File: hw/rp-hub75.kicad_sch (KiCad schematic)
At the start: 39 parts, among them J1 Display Connector, J2 USB_C_Receptacle_USB2.0_16P, J3 Screw_Terminal_01x02, J5 USB_A, J6 Conn_01x10, J7 Conn_01x05, J8 Conn_01x04, SW1 SW_Push, U1 AMS1117-3.3, U2 RP2350_60QFN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

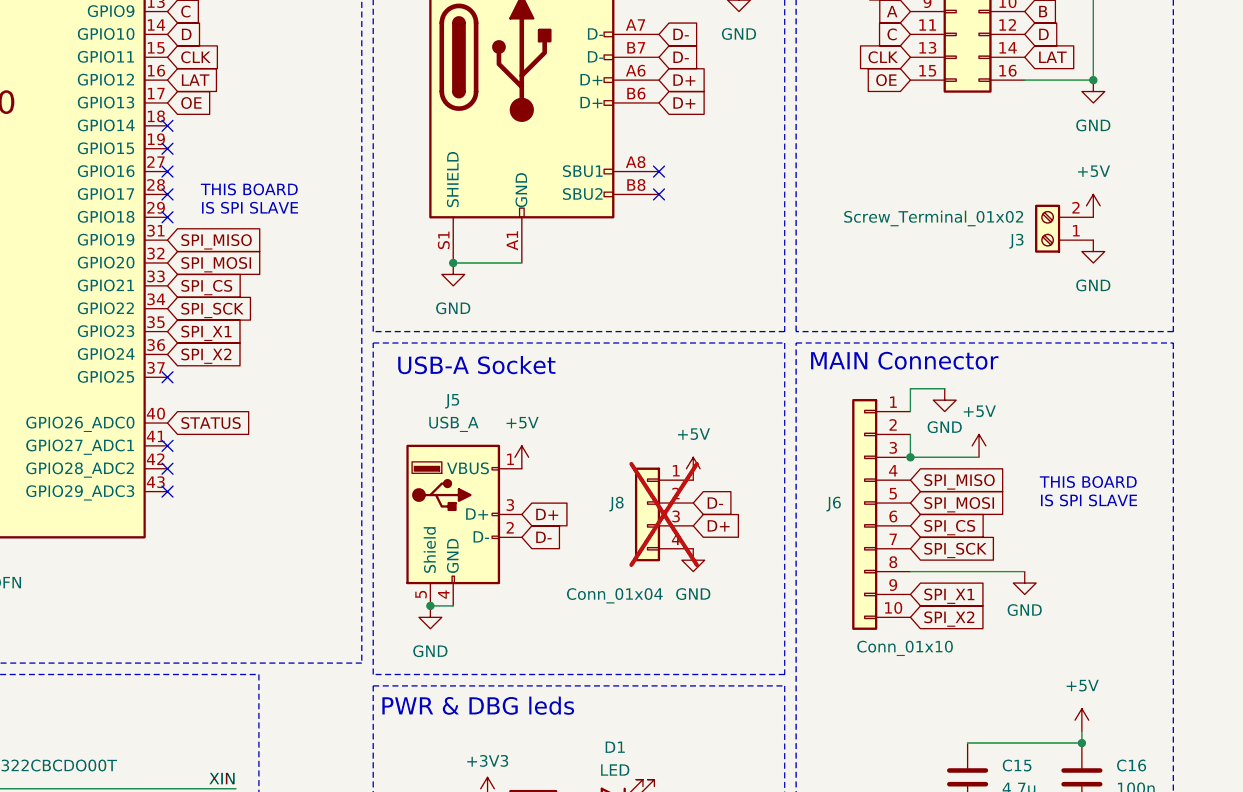
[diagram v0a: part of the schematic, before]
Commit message: v1.5 - use QSPI, better 1V1 line
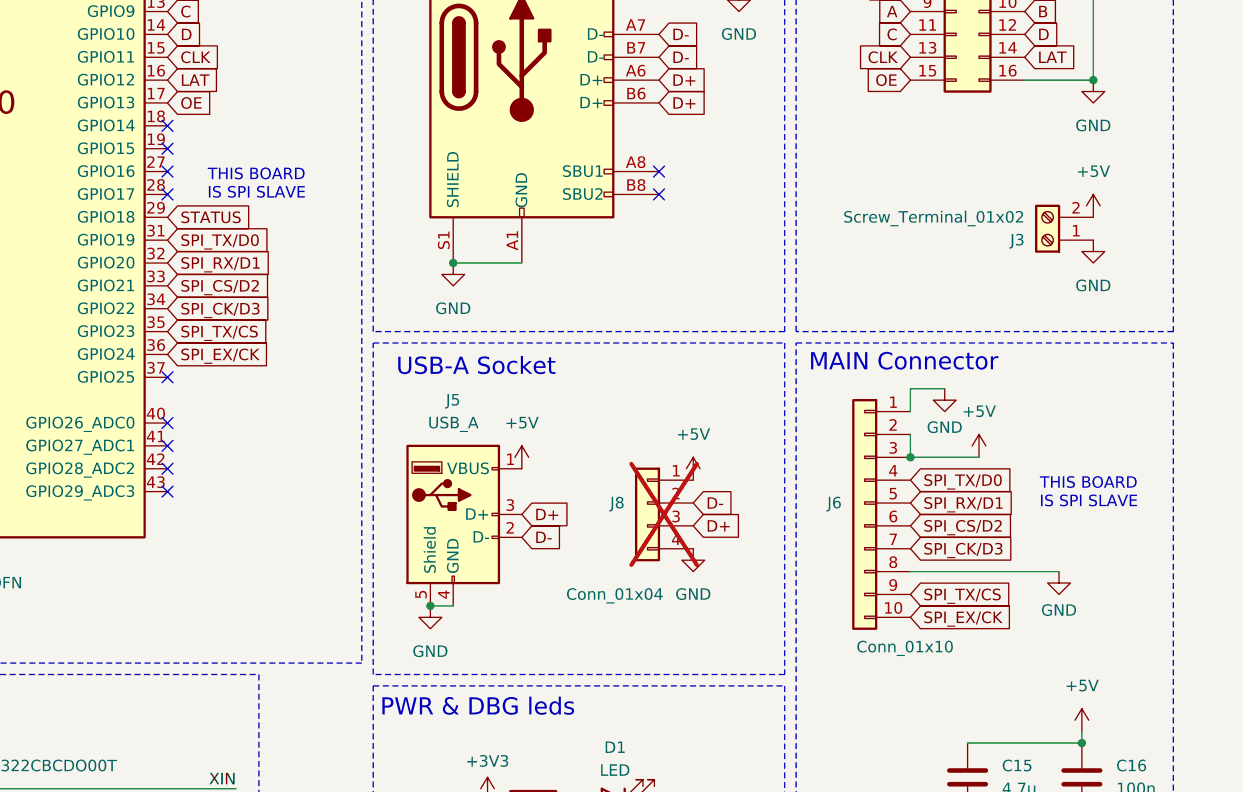
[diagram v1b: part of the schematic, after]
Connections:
- net STATUS: now also U2.29 (GPIO18); no longer U2.40 (GPIO26_ADC0)
- net SPI_CS renamed SPI_CS/D2
- net SPI_MISO renamed SPI_TX/D0
- net SPI_MOSI renamed SPI_RX/D1
- net SPI_SCK renamed SPI_CK/D3
- net SPI_X1 renamed SPI_TX/CS
- net SPI_X2 renamed SPI_EX/CK

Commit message: v1.6
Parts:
- removed J8: Conn_01x04, Connector_PinHeader_2.54mm:PinHeader_1x04_P2.54mm_Vertical, symbol Connector_Generic:Conn_01x04
- added J4: Conn_01x03, Connector_PinHeader_2.54mm:PinHeader_1x03_P2.54mm_Vertical, symbol Connector_Generic:Conn_01x03
- J3, J5: now not fitted
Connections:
- net GND: now also J4.1 (Pin_1)
- net SDA: now reaches U2.18 (GPIO14)
- net SDA: now also J4.3 (Pin_3)
- net SCL: now reaches U2.19 (GPIO15)
- net SCL: now also J4.2 (Pin_2)
- no-connect marks 11 -> 9

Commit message: v1.7
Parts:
- removed J6: Conn_01x10, Connector_JST:JST_XH_S10B-XH-A-1_1x10_P2.50mm_Horizontal, symbol Connector_Generic:Conn_01x10
- added J8: ZX-XH2.54-10PWT, Library:JST-XH-SMD-10Pin, symbol Connector_Generic_MountingPin:Conn_01x10_MountingPin
- J3: now fitted
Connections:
- net +5V: now also J8.2 (Pin_2), J8.3 (Pin_3)
- net GND: now also J8.1 (Pin_1), J8.8 (Pin_8), J8.MP (MountPin)
- net SPI_CK/D3: now also J8.7 (Pin_7)
- net SPI_CS/D2: now also J8.6 (Pin_6)
- net SPI_EX/CK: now also J8.10 (Pin_10)
- net SPI_RX/D1: now also J8.5 (Pin_5)
- net SPI_TX/CS: now also J8.9 (Pin_9)
- net SPI_TX/D0: now also J8.4 (Pin_4)
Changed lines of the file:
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@@
 	)
 	(junction
-		(at 271.78 176.53)
-		(diameter 0)
-		(color 0 0 0 0)
-	)
-	(junction
 		(at 218.44 193.04)
 		(diameter 0)
@@
 	)
 	(junction
+		(at 271.78 176.53)
+		(diameter 0)
+		(color 0 0 0 0)
+	)
+	(junction
 		(at 170.18 85.09)
 		(diameter 0)
@@
 		(on_board yes)
 		(in_pos_files yes)
-		(dnp yes)
+		(dnp no)
 		(property "Reference" "J3"
 			(at 284.48 152.4001 0)
@@
 	)
 	(symbol
-		(lib_id "Connector_Generic:Conn_01x10")
-		(at 266.7 181.61 0)
-		(mirror y)
-		(unit 1)
-		(body_style 1)
-		(exclude_from_sim no)
-		(in_bom yes)
-		(on_board yes)
-		(in_pos_files yes)
-		(dnp no)
-		(property "Reference" "J6"
-			(at 264.16 181.6099 0)
-			(show_name no)
-			(do_not_autoplace no)
-			(effects
-				(font
-					(size 1.27 1.27)
-				)
-				(justify left)
-			)
-		)
-		(property "Value" "Conn_01x10"
-			(at 276.606 197.612 0)
-			(show_name no)
-			(do_not_autoplace no)
-			(effects
-				(font
-					(size 1.27 1.27)
-				)
-				(justify left)
-			)
-		)
-		(property "Footprint" "Connector_JST:JST_XH_S10B-XH-A-1_1x10_P2.50mm_Horizontal"
-			(at 266.7 181.61 0)
-			(hide yes)
-			(show_name no)
-			(do_not_autoplace no)
-			(effects
-				(font
-					(size 1.27 1.27)
-				)
-			)
-		)
-		(property "Datasheet" ""
-			(at 266.7 181.61 0)
-			(hide yes)
-			(show_name no)
-			(do_not_autoplace no)
-			(effects
-				(font
-					(size 1.27 1.27)
-				)
-			)
-		)
-		(property "Description" "Generic connector, single row, 01x10, script generated (kicad-library-utils/schlib/autogen/connector/)"
-			(at 266.7 181.61 0)
-			(hide yes)
-			(show_name no)
-			(do_not_autoplace no)
-			(effects
-				(font
-					(size 1.27 1.27)
-				)
-			)
-		)
-		(property "LCSC" "C491718"
-			(at 266.7 181.61 0)
-			(hide yes)
-			(show_name no)
-			(do_not_autoplace no)
-			(effects
-				(font
-					(size 1.27 1.27)
-				)
-			)
-		)
-		(pin "5"
-		)
-		(pin "1"
-		)
-		(pin "4"
-		)
-		(pin "9"
-		)
-		(pin "3"
-		)
-		(pin "10"
-		)
-		(pin "2"
-		)
-		(pin "6"
-		)
-		(pin "7"
-		)
-		(pin "8"
-		)
-		(instances
-			(project "rp-hub75"
-				(path "/b3849755-2bc4-4a7c-8e78-ae8190aa99e0"
-					(reference "J6")
-					(unit 1)
-				)
-			)
-		)
-	)
-	(symbol
 		(lib_id "power:GND")
 		(at 292.1 134.62 0)
@@
 	)
 	(symbol
+		(lib_id "power:GND")
+		(at 266.7 199.39 0)
+		(unit 1)
+		(body_style 1)
+		(exclude_from_sim no)
+		(in_bom yes)
+		(on_board yes)
+		(in_pos_files yes)
+		(dnp no)
+		(property "Reference" "#PWR040"
+			(at 266.7 205.74 0)
+			(hide yes)
+			(show_name no)
+			(do_not_autoplace no)
+			(effects
+				(font
+					(size 1.27 1.27)
+				)
+			)
+		)
+		(property "Value" "GND"
+			(at 266.7 203.708 0)
+			(show_name no)
+			(do_not_autoplace no)
+			(effects
+				(font
+					(size 1.27 1.27)
+				)
+			)
+		)
+		(property "Footprint" ""
+			(at 266.7 199.39 0)
+			(hide yes)
+			(show_name no)
+			(do_not_autoplace no)
+			(effects
+				(font
+					(size 1.27 1.27)
+				)
+			)
+		)
+		(property "Datasheet" ""
+			(at 266.7 199.39 0)
+			(hide yes)
+			(show_name no)
+			(do_not_autoplace no)
+			(effects
+				(font
+					(size 1.27 1.27)
+				)
+			)
+		)
+		(property "Description" "Power symbol creates a global label with name \"GND\" , ground"
+			(at 266.7 199.39 0)
+			(hide yes)
+			(show_name no)
+			(do_not_autoplace no)
+			(effects
+				(font
+					(size 1.27 1.27)
+				)
+			)
+		)
+		(pin "1"
+		)
+		(instances
+			(project "rp-hub75"
+				(path "/b3849755-2bc4-4a7c-8e78-ae8190aa99e0"
+					(reference "#PWR040")
+					(unit 1)
+				)
+			)
+		)
+	)
+	(symbol
 		(lib_id "power:+3V3")
 		(at 224.79 214.63 0)
@@
 					(unit 1)
 				)
+			)
+		)
+	)
+	(symbol
+		(lib_id "Connector_Generic_MountingPin:Conn_01x10_MountingPin")
+		(at 266.7 181.61 0)
+		(mirror y)
+		(unit 1)
+		(body_style 1)
+		(exclude_from_sim no)
+		(in_bom yes)
+		(on_board yes)
+		(in_pos_files yes)
+		(dnp no)
+		(property "Reference" "J8"
+			(at 267.462 167.386 0)
+			(show_name no)
+			(do_not_autoplace no)
+			(effects
+				(font
+					(size 1.27 1.27)
+				)
+				(justify left)
+			)
+		)
+		(property "Value" "ZX-XH2.54-10PWT"
+			(at 273.304 163.83 0)
+			(hide yes)
+			(show_name no)
+			(do_not_autoplace no)
+			(effects
+				(font
+					(size 1.27 1.27)
+				)
+				(justify left)
+			)
+		)
+		(property "Footprint" "Library:JST-XH-SMD-10Pin"
+			(at 266.7 181.61 0)
+			(hide yes)
+			(show_name no)
+			(do_not_autoplace no)
+			(effects
+				(font
+					(size 1.27 1.27)
+				)
+			)
+		)
+		(property "Datasheet" ""
+			(at 266.7 181.61 0)
+			(hide yes)
+			(show_name no)
+			(do_not_autoplace no)
+			(effects
+				(font
+					(size 1.27 1.27)
+				)
+			)
+		)
+		(property "Description" "Generic connectable mounting pin connector, single row, 01x10, script generated (kicad-library-utils/schlib/autogen/connector/)"
+			(at 266.7 181.61 0)
+			(hide yes)
+			(show_name no)
+			(do_not_autoplace no)
+			(effects
+				(font
+					(size 1.27 1.27)
+				)
+			)
+		)
+		(property "LCSC" "C7429679"
+			(at 266.7 181.61 0)
+			(hide yes)
+			(show_name no)
+			(do_not_autoplace no)
+			(effects
+				(font
+					(size 1.27 1.27)
+				)
+			)
+		)
+		(property "JLCPCB_CORRECTION" ""
+			(at 266.7 181.61 0)
+			(hide yes)
+			(show_name no)
+			(do_not_autoplace no)
+			(effects
+				(font
+					(size 1.27 1.27)
+				)
+			)
+		)
+		(pin "5"
+		)
+		(pin "1"
+		)
+		(pin "4"
+		)
+		(pin "9"
+		)
+		(pin "3"
+		)
+		(pin "10"
+		)
+		(pin "2"
+		)
+		(pin "6"
+		)
+		(pin "7"
+		)
+		(pin "8"
+		)
+		(pin "MP"
+		)
+		(instances
+			(project "rp-hub75"
+				(path "/b3849755-2bc4-4a7c-8e78-ae8190aa99e0"
+					(reference "J8")
+					(unit 1)
+				)
